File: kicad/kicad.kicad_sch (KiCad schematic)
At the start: 198 parts, among them J1 USB_B_Micro, J2 SWD, J3 pwr_led+, J4 pwr_led-, J5 caps_led+, J6 caps_led-, U1 AMS1117-3.3, Y1 16MGz, sw1 Esc, sw10 Z, sw11 LCtrl, sw12 LSys, sw13 F2, sw14 F3, sw15 2, sw16 3, sw17 W, sw18 E, sw19 S, sw2 F1, sw20 D, sw21 X, sw22 C, sw23 LAlt, sw24 THome, sw25 F4, sw26 F5, sw27 4, sw28 5, sw29 R, sw3 Tilda, sw30 T, sw31 F, sw32 G, sw33 V, sw34 B, sw35 LSpace, sw36 TLeft, sw37 F6, sw38 F7, sw39 6, sw4 1, sw40 7, sw41 Y, sw42 U, sw43 H, sw44 J, sw45 N, sw46 M, sw47 TUp, sw48 TDown, sw49 F8, sw5 Tab, sw50 F9, sw51 8, sw52 9, sw53 I, sw54 O, sw55 K, sw56 L, sw57 Comma, sw58 Period, sw59 RSpace, sw6 Q, sw60 TRight, sw61 F10, sw62 F11, sw63 0, sw64 Minus, sw65 P, sw66 LBrack, sw67 Semi, sw68 Quote, sw69 FSlash, sw7 CAPS, sw70 RShift, sw71 RAlt, sw72 TEnd, sw73 F12, sw74 PrtSc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

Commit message: change line endings
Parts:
- removed J2: SWD, Connector_PinHeader_2.54mm:PinHeader_1x04_P2.54mm_Vertical, symbol Connector:Conn_01x04_Male
- added J2: Conn_01x06_Pin, symbol Connector:Conn_01x06_Pin
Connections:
- net +3.3V: now also J2.6 (Pin_6)
- net GND: now also J2.1 (Pin_1)
- net NRST: now also J2.2 (Pin_2)
- net SWCLK: now also J2.4 (Pin_4)
- net SWDIO: now also J2.5 (Pin_5)
- net SWO: now reaches MCU1.55 (PB3)
- net SWO: now also J2.3 (Pin_3)
- no-connect marks 22 -> 21
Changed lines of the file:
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@@
   (junction (at 125.73 173.99) (diameter 0) (color 0 0 0 0)
   )
-  (no_connect (at 381 125.73))
   (no_connect (at 381 140.97))
   (no_connect (at 345.44 118.11))
@@
     (stroke (width 0) (type default))
   )
-  (wire (pts (xy 447.04 127) (xy 417.83 127))
+  (wire (pts (xy 417.83 127) (xy 447.04 127))
     (stroke (width 0) (type default))
   )
@@
     (stroke (width 0) (type default))
   )
-  (wire (pts (xy 444.5 132.08) (xy 444.5 135.89))
+  (wire (pts (xy 444.5 137.16) (xy 444.5 140.97))
     (stroke (width 0) (type default))
   )
@@
     (stroke (width 0) (type default))
   )
+  (wire (pts (xy 396.24 132.08) (xy 396.24 125.73))
+    (stroke (width 0) (type default))
+  )
   (wire (pts (xy 152.4 180.34) (xy 152.4 187.96))
     (stroke (width 0) (type default))
@@
     (stroke (width 0) (type default))
   )
+  (wire (pts (xy 396.24 125.73) (xy 381 125.73))
+    (stroke (width 0) (type default))
+  )
   (wire (pts (xy 25.4 109.22) (xy 38.1 109.22))
     (stroke (width 0) (type default))
@@
     (stroke (width 0) (type default))
   )
-  (wire (pts (xy 447.04 132.08) (xy 444.5 132.08))
-    (stroke (width 0) (type default))
-  )
   (wire (pts (xy 177.8 180.34) (xy 190.5 180.34))
     (stroke (width 0) (type default))
@@
     (stroke (width 0) (type default))
   )
+  (wire (pts (xy 412.75 129.54) (xy 447.04 129.54))
+    (stroke (width 0) (type default))
+  )
   (wire (pts (xy 163.83 138.43) (xy 163.83 156.21))
     (stroke (width 0) (type default))
@@
     (stroke (width 0) (type default))
   )
+  (wire (pts (xy 444.5 137.16) (xy 447.04 137.16))
+    (stroke (width 0) (type default))
+  )
   (wire (pts (xy 290.83 95.25) (xy 285.75 95.25))
     (stroke (width 0) (type default))
@@
     (stroke (width 0) (type default))
   )
-  (wire (pts (xy 447.04 129.54) (xy 412.75 129.54))
-    (stroke (width 0) (type default))
-  )
   (wire (pts (xy 49.53 120.65) (xy 49.53 138.43))
     (stroke (width 0) (type default))
@@
     (stroke (width 0) (type default))
   )
+  (wire (pts (xy 447.04 132.08) (xy 396.24 132.08))
+    (stroke (width 0) (type default))
+  )
   (wire (pts (xy 162.56 99.06) (xy 162.56 102.87))
     (stroke (width 0) (type default))
@@
     (effects (font (size 1.27 1.27)) (justify left bottom))
   )
+  (label "SWO" (at 398.78 132.08 0) (fields_autoplaced)
+    (effects (font (size 1.27 1.27)) (justify left bottom))
+  )
   (label "NRST" (at 330.2 67.31 0) (fields_autoplaced)
     (effects (font (size 1.27 1.27)) (justify left bottom))
@@
     )
   )
+  (global_label "NRST" (shape input) (at 447.04 134.62 180) (fields_autoplaced)
+    (effects (font (size 1.27 1.27)) (justify right))
+    (property "Intersheetrefs" "${INTERSHEET_REFS}" (at 439.3566 134.62 0)
+      (effects (font (size 1.27 1.27)) (justify right) hide)
+    )
+  )
   (global_label "ROW9" (shape input) (at 381 85.09 0) (fields_autoplaced)
     (effects (font (size 1.27 1.27)) (justify left))
@@
     )
   )
-  (symbol (lib_id "power:GND") (at 444.5 135.89 0) (unit 1)
+  (symbol (lib_id "power:GND") (at 444.5 140.97 0) (unit 1)
     (in_bom yes) (on_board yes) (dnp no) (fields_autoplaced)
-    (property "Reference" "#PWR0112" (at 444.5 142.24 0)
+    (property "Reference" "#PWR0112" (at 444.5 147.32 0)
       (effects (font (size 1.27 1.27)) hide)
     )
-    (property "Value" "GND" (at 444.5 140.97 0)
+    (property "Value" "GND" (at 444.5 146.05 0)
       (effects (font (size 1.27 1.27)) hide)
     )
-    (property "Footprint" "" (at 444.5 135.89 0)
+    (property "Footprint" "" (at 444.5 140.97 0)
       (effects (font (size 1.27 1.27)) hide)
     )
-    (property "Datasheet" "" (at 444.5 135.89 0)
+    (property "Datasheet" "" (at 444.5 140.97 0)
       (effects (font (size 1.27 1.27)) hide)
     )
@@
     )
   )
-  (symbol (lib_id "Connector:Conn_01x04_Male") (at 452.12 127 0) (mirror y) (unit 1)
-    (in_bom yes) (on_board yes) (dnp no) (fields_autoplaced)
-    (property "Reference" "J2" (at 453.39 126.9999 0)
-      (effects (font (size 1.27 1.27)) (justify right))
-    )
-    (property "Value" "SWD" (at 453.39 129.5399 0)
-      (effects (font (size 1.27 1.27)) (justify right))
-    )
-    (property "Footprint" "Connector_PinHeader_2.54mm:PinHeader_1x04_P2.54mm_Vertical" (at 452.12 127 0)
-      (effects (font (size 1.27 1.27)) hide)
-    )
-    (property "Datasheet" "~" (at 452.12 127 0)
-      (effects (font (size 1.27 1.27)) hide)
-    )
-    (pin "1")
-    (pin "2")
-    (pin "3")
-    (pin "4")
-    (instances
-      (project "kicad"
-        (path "/c4e33b41-37f7-4b97-829f-31876b272ced"
-          (reference "J2") (unit 1)
-        )
-      )
-    )
-  )
   (symbol (lib_id "Switch:SW_Push") (at 30.48 134.62 0) (unit 1)
     (in_bom yes) (on_board yes) (dnp no) (fields_autoplaced)
@@
         )
       )
+    )
+  )
+  (symbol (lib_id "Connector:Conn_01x06_Pin") (at 452.12 132.08 180) (unit 1)
+    (in_bom yes) (on_board yes) (dnp no) (fields_autoplaced)
+    (property "Reference" "J2" (at 453.39 130.175 0)
+      (effects (font (size 1.27 1.27)) (justify right))
+    )
+    (property "Value" "Conn_01x06_Pin" (at 453.39 132.715 0)
+      (effects (font (size 1.27 1.27)) (justify right))
+    )
+    (property "Footprint" "" (at 452.12 132.08 0)
+      (effects (font (size 1.27 1.27)) hide)
+    )
+    (property "Datasheet" "~" (at 452.12 132.08 0)
+      (effects (font (size 1.27 1.27)) hide)
+    )
+    (pin "1")
+    (pin "2")
+    (pin "3")
+    (pin "4")
+    (pin "5")
+    (pin "6")
+    (instances
+      (project "kicad"
+        (path "/c4e33b41-37f7-4b97-829f-31876b272ced"
+          (reference "J2") (unit 1)
+        )
+      )

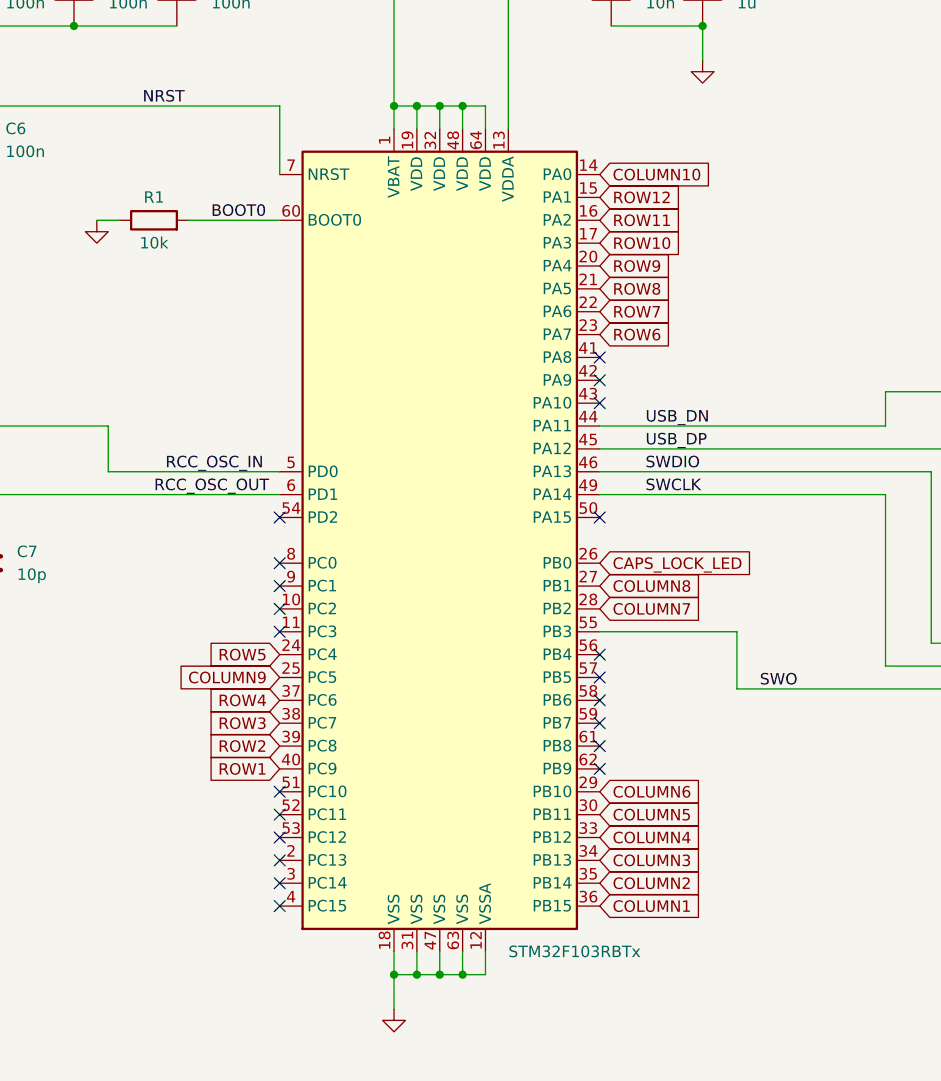
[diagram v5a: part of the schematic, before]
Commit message: connect grid to mcu
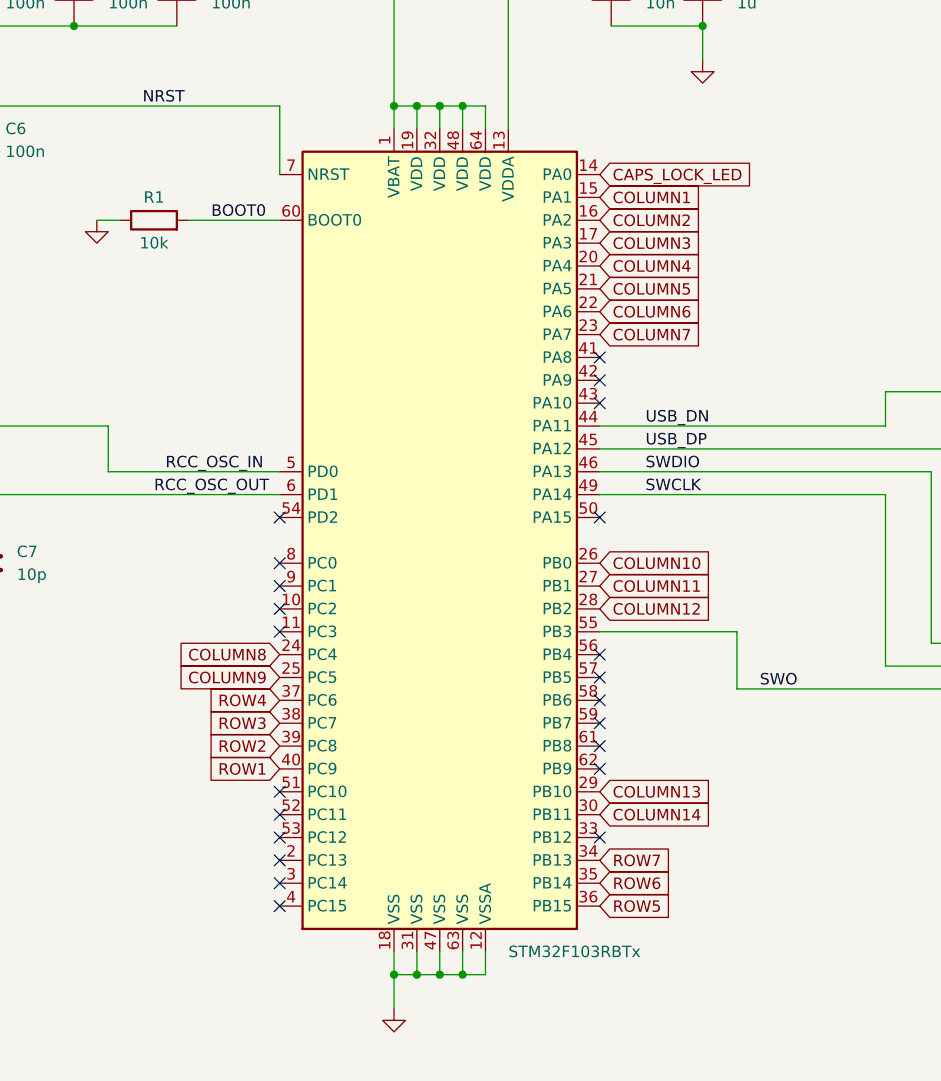
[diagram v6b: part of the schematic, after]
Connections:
- net ROW10 is gone; now on net COLUMN3: MCU1.17 (PA3)
- net ROW11 is gone; now on net COLUMN2: MCU1.16 (PA2)
- net ROW12 is gone; now on net COLUMN1: MCU1.15 (PA1)
- net ROW8 is gone; now on net COLUMN5: MCU1.21 (PA5)
- net ROW9 is gone; now on net COLUMN4: MCU1.20 (PA4)
- net CAPS_LOCK_LED: now also MCU1.14 (PA0); no longer MCU1.26 (PB0)
- net COLUMN1: no longer MCU1.36 (PB15)
- net COLUMN10: now also MCU1.26 (PB0); no longer MCU1.14 (PA0)
- net COLUMN11: now also MCU1.27 (PB1)
- net COLUMN12: now also MCU1.28 (PB2)
- net COLUMN13: now also MCU1.29 (PB10)
- net COLUMN14: now also MCU1.30 (PB11)
- net COLUMN2: no longer MCU1.35 (PB14)
- net COLUMN3: no longer MCU1.34 (PB13)
- net COLUMN4: no longer MCU1.33 (PB12)
- net COLUMN5: no longer MCU1.30 (PB11)
- net COLUMN6: now also MCU1.22 (PA6); no longer MCU1.29 (PB10)
- net COLUMN7: now also MCU1.23 (PA7); no longer MCU1.28 (PB2)
- net COLUMN8: now also MCU1.24 (PC4); no longer MCU1.27 (PB1)
- net ROW5: now also MCU1.36 (PB15); no longer MCU1.24 (PC4)
- net ROW6: now also MCU1.35 (PB14); no longer MCU1.23 (PA7)
- net ROW7: now also MCU1.34 (PB13); no longer MCU1.22 (PA6)
- no-connect marks 21 -> 22
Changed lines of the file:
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@@
   (no_connect (at 345.44 143.51))
   (no_connect (at 381 113.03))
+  (no_connect (at 381 148.59))
   (no_connect (at 381 100.33))
   (no_connect (at 345.44 123.19))
@@
     )
   )
-  (global_label "COLUMN7" (shape input) (at 381 123.19 0) (fields_autoplaced)
-    (effects (font (size 1.27 1.27)) (justify left))
-    (property "Intersheetrefs" "${INTERSHEET_REFS}" (at 392.3636 123.1106 0)
+  (global_label "COLUMN7" (shape input) (at 381 92.71 0) (fields_autoplaced)
+    (effects (font (size 1.27 1.27)) (justify left))
+    (property "Intersheetrefs" "${INTERSHEET_REFS}" (at 392.3636 92.6306 0)
       (effects (font (size 1.27 1.27)) (justify left) hide)
     )
@@
     )
   )
-  (global_label "ROW10" (shape input) (at 381 82.55 0) (fields_autoplaced)
-    (effects (font (size 1.27 1.27)) (justify left))
-    (property "Intersheetrefs" "${INTERSHEET_REFS}" (at 389.8841 82.4706 0)
-      (effects (font (size 1.27 1.27)) (justify left) hide)
-    )
-  )
-  (global_label "COLUMN4" (shape input) (at 381 148.59 0) (fields_autoplaced)
-    (effects (font (size 1.27 1.27)) (justify left))
-    (property "Intersheetrefs" "${INTERSHEET_REFS}" (at 392.3636 148.5106 0)
-      (effects (font (size 1.27 1.27)) (justify left) hide)
-    )
-  )
-  (global_label "ROW7" (shape input) (at 381 90.17 0) (fields_autoplaced)
-    (effects (font (size 1.27 1.27)) (justify left))
-    (property "Intersheetrefs" "${INTERSHEET_REFS}" (at 388.6745 90.0906 0)
+  (global_label "COLUMN11" (shape input) (at 381 120.65 0) (fields_autoplaced)
+    (effects (font (size 1.27 1.27)) (justify left))
+    (property "Intersheetrefs" "${INTERSHEET_REFS}" (at 394.0658 120.65 0)
+      (effects (font (size 1.27 1.27)) (justify left) hide)
+    )
+  )
+  (global_label "ROW7" (shape input) (at 381 151.13 0) (fields_autoplaced)
+    (effects (font (size 1.27 1.27)) (justify left))
+    (property "Intersheetrefs" "${INTERSHEET_REFS}" (at 388.6745 151.0506 0)
       (effects (font (size 1.27 1.27)) (justify left) hide)
     )
@@
     )
   )
-  (global_label "CAPS_LOCK_LED" (shape input) (at 381 118.11 0) (fields_autoplaced)
-    (effects (font (size 1.27 1.27)) (justify left))
-    (property "Intersheetrefs" "${INTERSHEET_REFS}" (at 398.5321 118.0306 0)
+  (global_label "CAPS_LOCK_LED" (shape input) (at 381 74.93 0) (fields_autoplaced)
+    (effects (font (size 1.27 1.27)) (justify left))
+    (property "Intersheetrefs" "${INTERSHEET_REFS}" (at 398.5321 74.8506 0)
       (effects (font (size 1.27 1.27)) (justify left) hide)
     )
@@
     )
   )
-  (global_label "COLUMN8" (shape input) (at 381 120.65 0) (fields_autoplaced)
-    (effects (font (size 1.27 1.27)) (justify left))
-    (property "Intersheetrefs" "${INTERSHEET_REFS}" (at 392.3636 120.5706 0)
-      (effects (font (size 1.27 1.27)) (justify left) hide)
+  (global_label "COLUMN8" (shape input) (at 345.44 128.27 180) (fields_autoplaced)
+    (effects (font (size 1.27 1.27)) (justify right))
+    (property "Intersheetrefs" "${INTERSHEET_REFS}" (at 333.5837 128.27 0)
+      (effects (font (size 1.27 1.27)) (justify right) hide)
     )
   )
@@
     )
   )
-  (global_label "ROW9" (shape input) (at 381 85.09 0) (fields_autoplaced)
-    (effects (font (size 1.27 1.27)) (justify left))
-    (property "Intersheetrefs" "${INTERSHEET_REFS}" (at 388.6745 85.0106 0)
+  (global_label "COLUMN13" (shape input) (at 381 143.51 0) (fields_autoplaced)
+    (effects (font (size 1.27 1.27)) (justify left))
+    (property "Intersheetrefs" "${INTERSHEET_REFS}" (at 394.0658 143.51 0)
       (effects (font (size 1.27 1.27)) (justify left) hide)
     )
@@
     )
   )
-  (global_label "COLUMN3" (shape input) (at 381 151.13 0) (fields_autoplaced)
-    (effects (font (size 1.27 1.27)) (justify left))
-    (property "Intersheetrefs" "${INTERSHEET_REFS}" (at 392.3636 151.0506 0)
-      (effects (font (size 1.27 1.27)) (justify left) hide)
-    )
-  )
-  (global_label "COLUMN10" (shape input) (at 381 74.93 0) (fields_autoplaced)
-    (effects (font (size 1.27 1.27)) (justify left))
-    (property "Intersheetrefs" "${INTERSHEET_REFS}" (at 393.5731 74.8506 0)
+  (global_label "COLUMN3" (shape input) (at 381 82.55 0) (fields_autoplaced)
+    (effects (font (size 1.27 1.27)) (justify left))
+    (property "Intersheetrefs" "${INTERSHEET_REFS}" (at 392.3636 82.4706 0)
+      (effects (font (size 1.27 1.27)) (justify left) hide)
+    )
+  )
+  (global_label "COLUMN10" (shape input) (at 381 118.11 0) (fields_autoplaced)
+    (effects (font (size 1.27 1.27)) (justify left))
+    (property "Intersheetrefs" "${INTERSHEET_REFS}" (at 394.0658 118.11 0)
       (effects (font (size 1.27 1.27)) (justify left) hide)
     )
@@
     )
   )
-  (global_label "ROW8" (shape input) (at 381 87.63 0) (fields_autoplaced)
-    (effects (font (size 1.27 1.27)) (justify left))
-    (property "Intersheetrefs" "${INTERSHEET_REFS}" (at 388.6745 87.5506 0)
-      (effects (font (size 1.27 1.27)) (justify left) hide)
-    )
-  )
-  (global_label "COLUMN2" (shape input) (at 381 153.67 0) (fields_autoplaced)
-    (effects (font (size 1.27 1.27)) (justify left))
-    (property "Intersheetrefs" "${INTERSHEET_REFS}" (at 392.3636 153.7494 0)
-      (effects (font (size 1.27 1.27)) (justify left) hide)
-    )
-  )
-  (global_label "ROW12" (shape input) (at 381 77.47 0) (fields_autoplaced)
-    (effects (font (size 1.27 1.27)) (justify left))
-    (property "Intersheetrefs" "${INTERSHEET_REFS}" (at 389.8841 77.3906 0)
+  (global_label "COLUMN14" (shape input) (at 381 146.05 0) (fields_autoplaced)
+    (effects (font (size 1.27 1.27)) (justify left))
+    (property "Intersheetrefs" "${INTERSHEET_REFS}" (at 394.0658 146.05 0)
+      (effects (font (size 1.27 1.27)) (justify left) hide)
+    )
+  )
+  (global_label "COLUMN2" (shape input) (at 381 80.01 0) (fields_autoplaced)
+    (effects (font (size 1.27 1.27)) (justify left))
+    (property "Intersheetrefs" "${INTERSHEET_REFS}" (at 392.3636 80.0894 0)
+      (effects (font (size 1.27 1.27)) (justify left) hide)
+    )
+  )
+  (global_label "COLUMN4" (shape input) (at 381 85.09 0) (fields_autoplaced)
+    (effects (font (size 1.27 1.27)) (justify left))
+    (property "Intersheetrefs" "${INTERSHEET_REFS}" (at 392.8563 85.09 0)
       (effects (font (size 1.27 1.27)) (justify left) hide)
     )
@@
     )
   )
-  (global_label "ROW6" (shape input) (at 381 92.71 0) (fields_autoplaced)
-    (effects (font (size 1.27 1.27)) (justify left))
-    (property "Intersheetrefs" "${INTERSHEET_REFS}" (at 388.6745 92.6306 0)
-      (effects (font (size 1.27 1.27)) (justify left) hide)
-    )
-  )
-  (global_label "COLUMN1" (shape input) (at 381 156.21 0) (fields_autoplaced)
-    (effects (font (size 1.27 1.27)) (justify left))
-    (property "Intersheetrefs" "${INTERSHEET_REFS}" (at 392.3636 156.2894 0)
+  (global_label "ROW6" (shape input) (at 381 153.67 0) (fields_autoplaced)
+    (effects (font (size 1.27 1.27)) (justify left))
+    (property "Intersheetrefs" "${INTERSHEET_REFS}" (at 388.6745 153.5906 0)
+      (effects (font (size 1.27 1.27)) (justify left) hide)
+    )
+  )
+  (global_label "COLUMN1" (shape input) (at 381 77.47 0) (fields_autoplaced)
+    (effects (font (size 1.27 1.27)) (justify left))
+    (property "Intersheetrefs" "${INTERSHEET_REFS}" (at 392.3636 77.5494 0)
       (effects (font (size 1.27 1.27)) (justify left) hide)
     )
@@
     )
   )
-  (global_label "ROW5" (shape input) (at 345.44 128.27 180) (fields_autoplaced)
-    (effects (font (size 1.27 1.27)) (justify right))
-    (property "Intersheetrefs" "${INTERSHEET_REFS}" (at 337.7655 128.3494 0)
-      (effects (font (size 1.27 1.27)) (justify right) hide)
-    )
-  )
-  (global_label "ROW11" (shape input) (at 381 80.01 0) (fields_autoplaced)
-    (effects (font (size 1.27 1.27)) (justify left))
-    (property "Intersheetrefs" "${INTERSHEET_REFS}" (at 389.8841 79.9306 0)
+  (global_label "ROW5" (shape input) (at 381 156.21 0) (fields_autoplaced)
+    (effects (font (size 1.27 1.27)) (justify left))
+    (property "Intersheetrefs" "${INTERSHEET_REFS}" (at 389.1672 156.21 0)
+      (effects (font (size 1.27 1.27)) (justify left) hide)
+    )
+  )
+  (global_label "COLUMN12" (shape input) (at 381 123.19 0) (fields_autoplaced)
+    (effects (font (size 1.27 1.27)) (justify left))
+    (property "Intersheetrefs" "${INTERSHEET_REFS}" (at 394.0658 123.19 0)
       (effects (font (size 1.27 1.27)) (justify left) hide)
     )
@@
     )
   )
-  (global_label "COLUMN6" (shape input) (at 381 143.51 0) (fields_autoplaced)
-    (effects (font (size 1.27 1.27)) (justify left))
-    (property "Intersheetrefs" "${INTERSHEET_REFS}" (at 392.3636 143.4306 0)
+  (global_label "COLUMN6" (shape input) (at 381 90.17 0) (fields_autoplaced)
+    (effects (font (size 1.27 1.27)) (justify left))
+    (property "Intersheetrefs" "${INTERSHEET_REFS}" (at 392.3636 90.0906 0)
       (effects (font (size 1.27 1.27)) (justify left) hide)
     )
@@
     )
   )
-  (global_label "COLUMN5" (shape input) (at 381 146.05 0) (fields_autoplaced)
-    (effects (font (size 1.27 1.27)) (justify left))
-    (property "Intersheetrefs" "${INTERSHEET_REFS}" (at 392.3636 145.9706 0)
-      (effects (font (size 1.27 1.27)) (justify left) hide)
-    )
+  (global_label "COLUMN5" (shape input) (at 381 87.63 0) (fields_autoplaced)
+    (effects (font (size 1.27 1.27)) (justify left))
+    (property "Intersheetrefs" "${INTERSHEET_REFS}" (at 392.3636 87.5506 0)
+      (effects (font (size 1.27 1.27)) (justify left) hide)
+    )
